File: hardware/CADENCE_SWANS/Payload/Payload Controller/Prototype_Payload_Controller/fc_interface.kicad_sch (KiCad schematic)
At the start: 9 parts

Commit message: clean up
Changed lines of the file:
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@@
 	(wire
 		(pts
-			(xy 44.45 82.55) (xy 52.07 82.55)
+			(xy 34.29 82.55) (xy 52.07 82.55)
 		)
 		(stroke
@@
 	(wire
 		(pts
-			(xy 44.45 69.85) (xy 53.34 69.85)
+			(xy 34.29 69.85) (xy 53.34 69.85)
 		)
 		(stroke
@@
 	(hierarchical_label "Payload_Rx"
 		(shape input)
-		(at 44.45 82.55 180)
+		(at 34.29 82.55 180)
 		(effects
 			(font
@@
 	(hierarchical_label "Payload_Tx"
 		(shape input)
-		(at 44.45 69.85 180)
+		(at 34.29 69.85 180)
 		(effects
 			(font

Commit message: minor updates
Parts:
- C2: value 10u -> 10uF
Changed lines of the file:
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@@
 			)
 		)
-		(property "Value" "10u"
+		(property "Value" "10uF"
 			(at 91.44 33.0262 0)
 			(effects

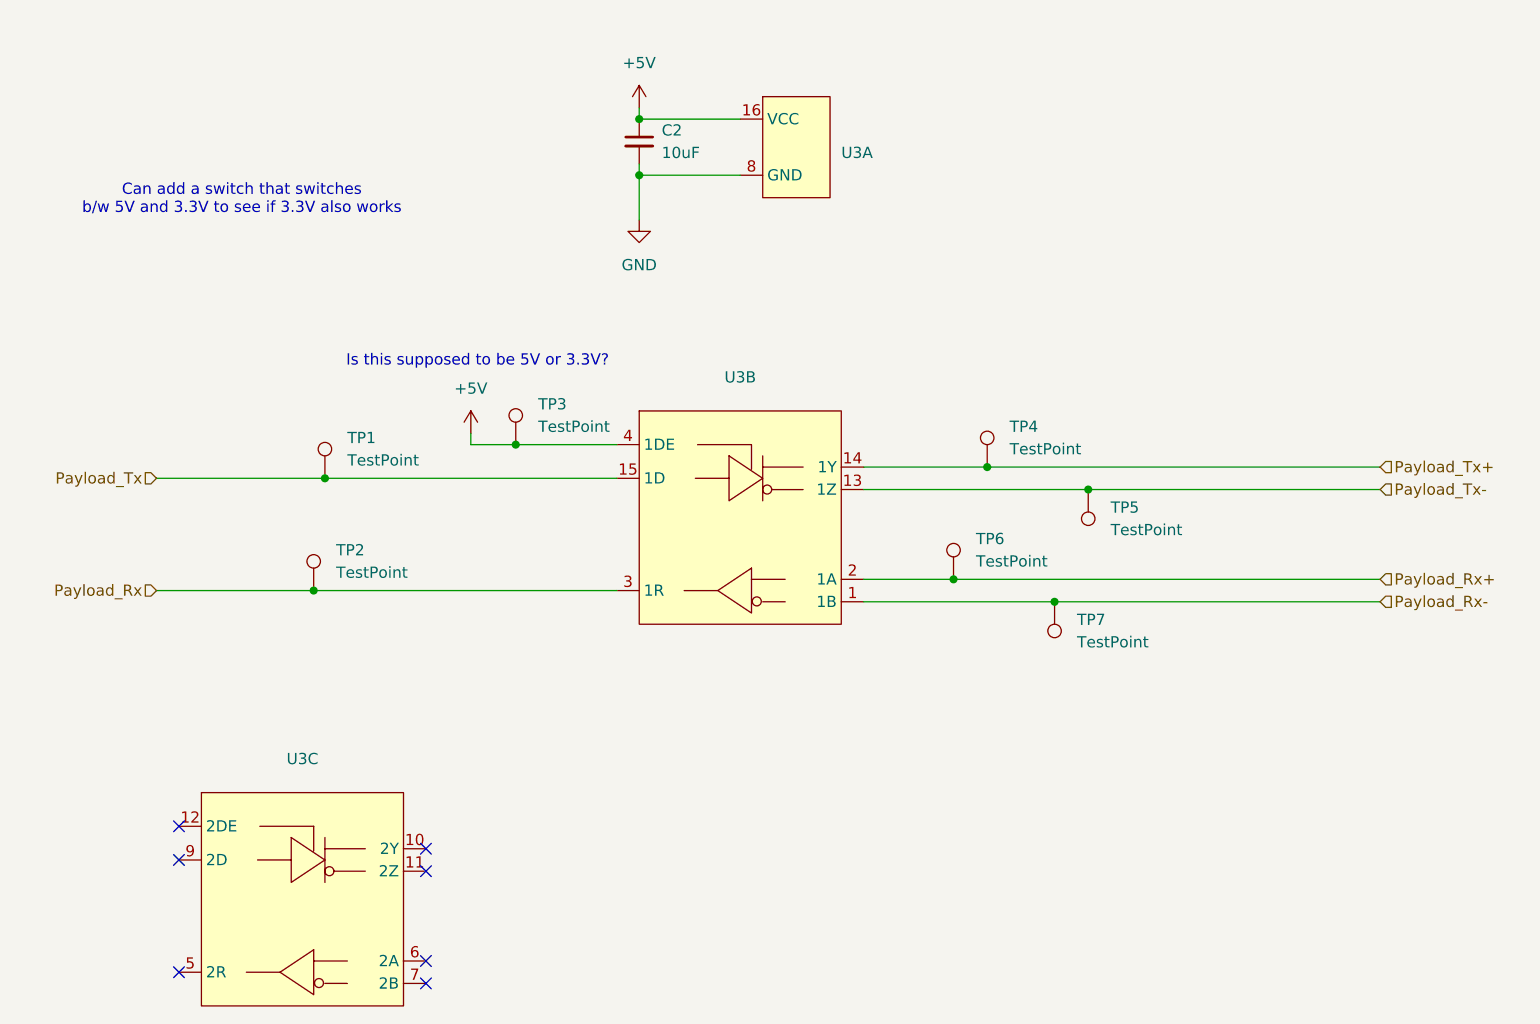
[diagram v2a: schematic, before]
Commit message: updated power regulators
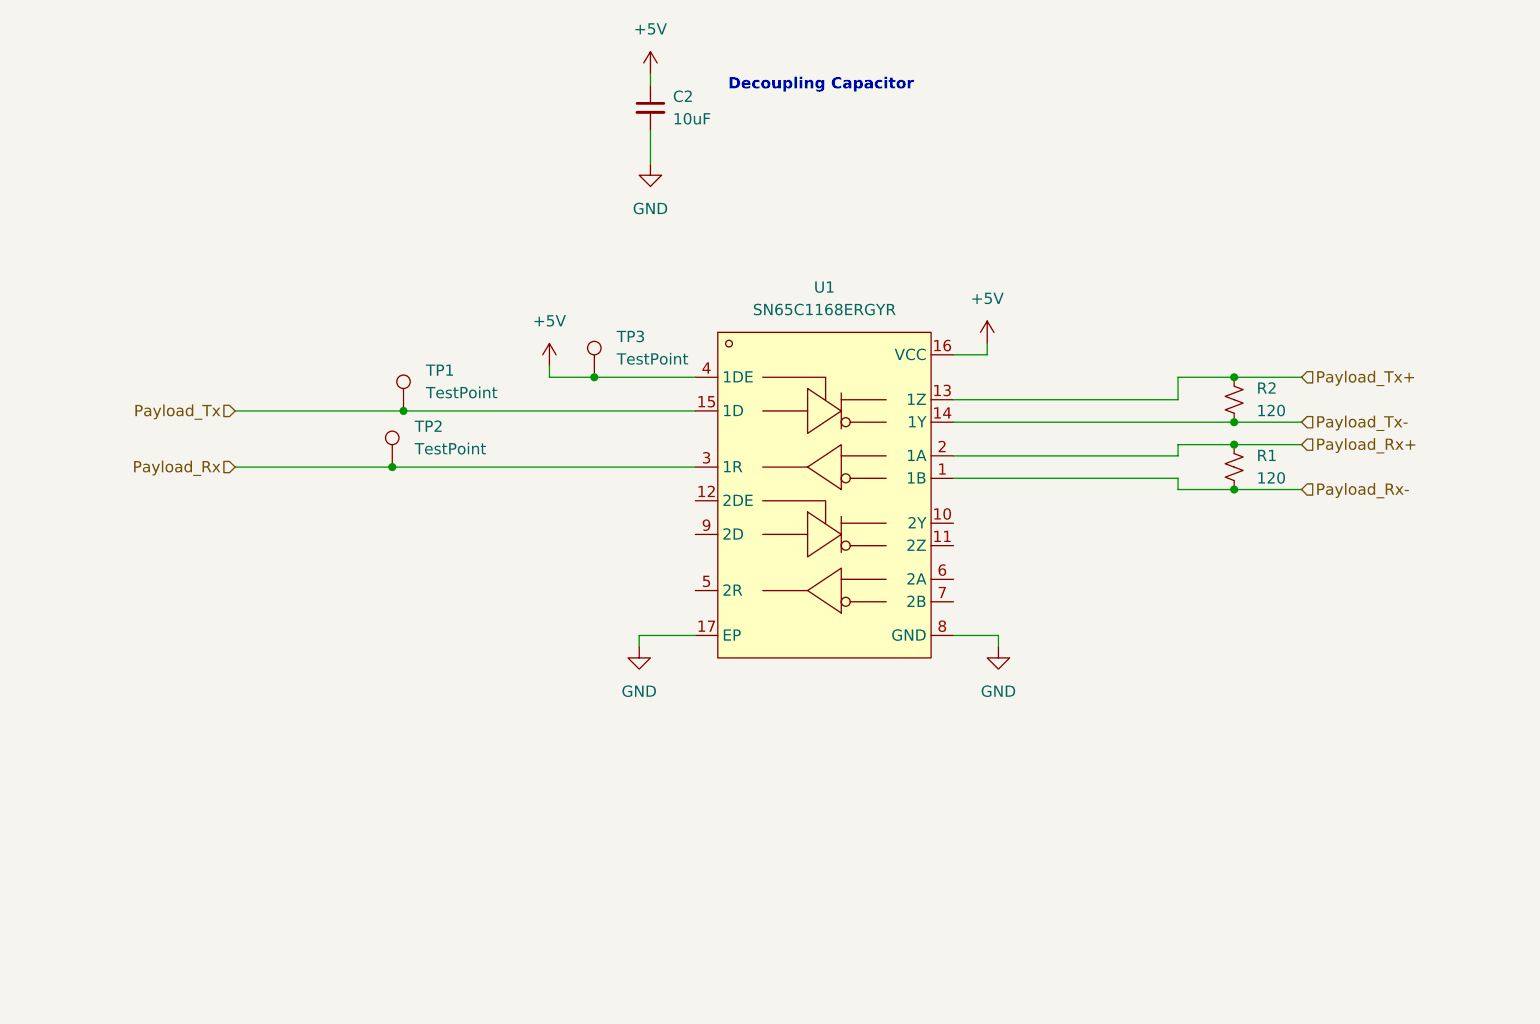
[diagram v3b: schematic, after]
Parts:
- removed TP4, TP5, TP6, TP7: TestPoint, symbol Connector:TestPoint
- removed U3: ~, symbol SN65C1168:SN65C1168
- added R1, R2: 120, symbol Device:R_Small_US
- added U1: SN65C1168ERGYR, easyeda2kicad:VQFN-16_L4.0-W3.5-P0.50-BL-EP, symbol CADENCE:SN65C1168ERGYR
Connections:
- net +5V: now also U1.16 (VCC), U1.4 (1DE)
- net GND: now also U1.17 (EP), U1.8 (GND)
- net Payload_Rx: now also U1.3 (1R)
- net Payload_Rx+: now also R1.1, U1.2 (1A)
- net Payload_Rx-: now also R1.2, U1.1 (1B)
- net Payload_Tx: now also U1.15 (1D)
- net Payload_Tx+: now also R2.1, U1.13 (1Z)
- net Payload_Tx-: now also R2.2, U1.14 (1Y)
- no-connect marks 7 -> 0
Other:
- note added: "Decoupling Capacitor"
- note removed: "Can add a switch that switches b/w 5V and 3.3V to see if 3.3V also works"
- note removed: "Is this supposed to be 5V or 3.3V?"
- moved on the sheet: C2, TP1, TP2, TP3

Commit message: cleaned up schematics and assigned footprints for resistors and capacitors
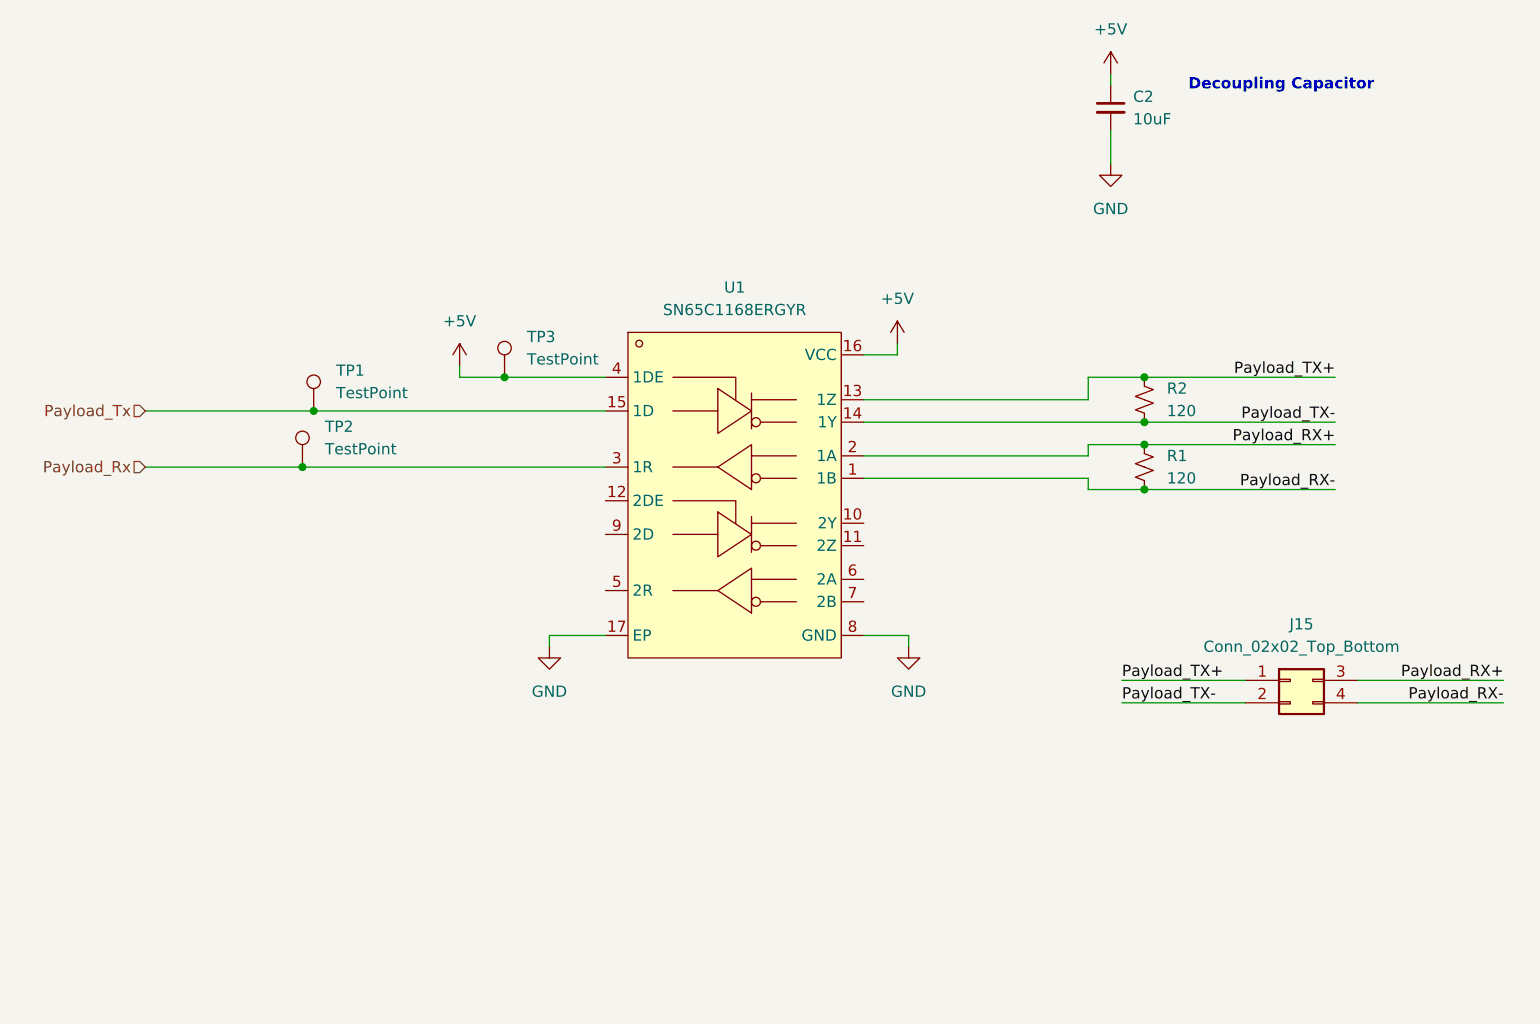
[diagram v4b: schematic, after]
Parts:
- added J15: Conn_02x02_Top_Bottom, symbol Connector_Generic:Conn_02x02_Top_Bottom
- C2: footprint (none) -> Capacitor_SMD:C_0603_1608Metric
- R1, R2: footprint (none) -> Resistor_SMD:R_0603_1608Metric
- TP1, TP2, TP3: footprint (none) -> TestPoint:TestPoint_Pad_1.0x1.0mm
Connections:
- net Payload_Rx+ renamed Payload_RX+
- net Payload_RX+: now also J15.3 (Pin_3)
- net Payload_Rx- renamed Payload_RX-
- net Payload_RX-: now also J15.4 (Pin_4)
- net Payload_Tx+ renamed Payload_TX+
- net Payload_TX+: now also J15.1 (Pin_1)
- net Payload_Tx- renamed Payload_TX-
- net Payload_TX-: now also J15.2 (Pin_2)
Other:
- moved on the sheet: C2, R1, R2, TP1, TP2, TP3, U1

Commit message: assigned more footprints
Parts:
- J15: footprint (none) -> Connector_Hirose:Hirose_DF11-4DP-2DSA_2x02_P2.00mm_Vertical
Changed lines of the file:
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@@
 			)
 		)
-		(property "Footprint" ""
+		(property "Footprint" "Connector_Hirose:Hirose_DF11-4DP-2DSA_2x02_P2.00mm_Vertical"
 			(at 162.56 92.71 0)
 			(effects

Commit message: removed termination resistor on transmitter end of RS422
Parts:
- removed R2: 120, Resistor_SMD:R_0603_1608Metric, symbol Device:R_Small_US
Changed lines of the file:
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@@
-	)
-	(junction
-		(at 146.05 58.42)
-		(diameter 0)
-		(color 0 0 0 0)
 	)
 	(junction
@@
 		(color 0 0 0 0)
 	)
-	(junction
-		(at 146.05 63.5)
-		(diameter 0)
-		(color 0 0 0 0)
-	)
 	(wire
 		(pts
@@
 	(wire
 		(pts
-			(xy 114.3 63.5) (xy 146.05 63.5)
+			(xy 114.3 63.5) (xy 167.64 63.5)
 		)
 		(stroke
@@
 	(wire
 		(pts
-			(xy 139.7 60.96) (xy 139.7 58.42)
-		)
-		(stroke
-			(width 0)
-			(type default)
-		)
-	)
-	(wire
-		(pts
 			(xy 118.11 55.88) (xy 118.11 54.61)
 		)
@@
 	(wire
 		(pts
-			(xy 139.7 58.42) (xy 146.05 58.42)
-		)
-		(stroke
-			(width 0)
-			(type default)
-		)
-	)
-	(wire
-		(pts
 			(xy 139.7 66.04) (xy 146.05 66.04)
 		)
@@
 	(wire
 		(pts
-			(xy 146.05 58.42) (xy 167.64 58.42)
-		)
-		(stroke
-			(width 0)
-			(type default)
-		)
-	)
-	(wire
-		(pts
-			(xy 146.05 63.5) (xy 167.64 63.5)
-		)
-		(stroke
-			(width 0)
-			(type default)
-		)
-	)
-	(wire
-		(pts
 			(xy 143.51 95.25) (xy 157.48 95.25)
 		)
@@
 	(wire
 		(pts
-			(xy 114.3 60.96) (xy 139.7 60.96)
+			(xy 114.3 60.96) (xy 167.64 60.96)
 		)
 		(stroke
@@
 	)
 	(label "Payload_TX+"
-		(at 167.64 58.42 180)
+		(at 167.64 60.96 180)
 		(effects
 			(font
@@
 					(unit 1)
 				)
-			)
-		)
-	)
-	(symbol
-		(lib_id "Device:R_Small_US")
-		(at 146.05 60.96 0)
-		(unit 1)
-		(exclude_from_sim no)
-		(in_bom yes)
-		(on_board yes)
-		(dnp no)
-		(fields_autoplaced yes)
-		(property "Reference" "R2"
-			(at 148.59 59.6899 0)
-			(effects
-				(font
-					(size 1.27 1.27)
-				)
-				(justify left)
-			)
-		)
-		(property "Value" "120"
-			(at 148.59 62.2299 0)
-			(effects
-				(font
-					(size 1.27 1.27)
-				)
-				(justify left)
-			)
-		)
-		(property "Footprint" "Resistor_SMD:R_0603_1608Metric"
-			(at 146.05 60.96 0)
-			(effects
-				(font
-					(size 1.27 1.27)
-				)
-				(hide yes)
-			)
-		)
-		(property "Datasheet" "~"
-			(at 146.05 60.96 0)
-			(effects
-				(font
-					(size 1.27 1.27)
-				)
-				(hide yes)
-			)
-		)
-		(property "Description" "Resistor, small US symbol"
-			(at 146.05 60.96 0)
-			(effects
-				(font
-					(size 1.27 1.27)
-				)
-				(hide yes)
-			)
-		)
-		(pin "1"
-		)
-		(pin "2"
-		)
-		(instances
-			(project "Payload_Controller_EM"
-				(path "/866a965d-c307-40b7-9977-69e77fc0dc82/7acf6d3b-d272-4af5-ad05-5ed10a438eac"
-					(reference "R2")
-					(unit 1)
-				)

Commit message: linked more footprints
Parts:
- U1: footprint easyeda2kicad:VQFN-16_L4.0-W3.5-P0.50-BL-EP -> Package_SO:SOP-16_4.55x10.3mm_P1.27mm
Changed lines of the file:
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@@
 			)
 		)
-		(property "Footprint" "easyeda2kicad:VQFN-16_L4.0-W3.5-P0.50-BL-EP"
+		(property "Footprint" "Package_SO:SOP-16_4.55x10.3mm_P1.27mm"
 			(at 94.234 94.742 0)
 			(effects

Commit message: resolved ERC errors
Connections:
- no-connect marks 0 -> 7
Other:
- moved on the sheet: C2
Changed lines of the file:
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@@
 	(text "Decoupling Capacitor"
 		(exclude_from_sim no)
-		(at 161.544 25.4 0)
+		(at 151.384 33.02 0)
 		(effects
 			(font
@@
 		(color 0 0 0 0)
 	)
+	(no_connect
+		(at 85.09 82.55)
+	)
+	(no_connect
+		(at 85.09 76.2)
+	)
+	(no_connect
+		(at 114.3 77.47)
+	)
+	(no_connect
+		(at 114.3 74.93)
+	)
+	(no_connect
+		(at 85.09 72.39)
+	)
+	(no_connect
+		(at 114.3 81.28)
+	)
+	(no_connect
+		(at 114.3 83.82)
+	)
 	(wire
 		(pts
@@
 	(wire
 		(pts
-			(xy 142.24 24.13) (xy 142.24 25.4)
+			(xy 132.08 31.75) (xy 132.08 33.02)
 		)
 		(stroke
@@
 	(wire
 		(pts
-			(xy 142.24 30.48) (xy 142.24 34.29)
+			(xy 132.08 38.1) (xy 132.08 41.91)
 		)
 		(stroke
@@
 	(symbol
 		(lib_id "Device:C_Small")
-		(at 142.24 27.94 0)
+		(at 132.08 35.56 0)
 		(unit 1)
 		(exclude_from_sim no)
@@
 		(dnp no)
 		(property "Reference" "C2"
-			(at 144.78 26.6762 0)
+			(at 134.62 34.2962 0)
 			(effects
 				(font
@@
 		)
 		(property "Value" "10uF"
-			(at 144.78 29.2162 0)
+			(at 134.62 36.8362 0)
 			(effects
 				(font
@@
 		)
 		(property "Footprint" "Capacitor_SMD:C_0603_1608Metric"
-			(at 142.24 27.94 0)
+			(at 132.08 35.56 0)
 			(effects
 				(font
@@
 		)
 		(property "Datasheet" "~"
-			(at 142.24 27.94 0)
+			(at 132.08 35.56 0)
 			(effects
 				(font
@@
 		)
 		(property "Description" "Unpolarized capacitor, small symbol"
-			(at 142.24 27.94 0)
+			(at 132.08 35.56 0)
 			(effects
 				(font
@@
 	(symbol
 		(lib_id "power:GND")
-		(at 142.24 34.29 0)
+		(at 132.08 41.91 0)
 		(unit 1)
 		(exclude_from_sim no)
@@
 		(fields_autoplaced yes)
 		(property "Reference" "#PWR015"
-			(at 142.24 40.64 0)
+			(at 132.08 48.26 0)
 			(effects
 				(font
@@
 		)
 		(property "Value" "GND"
-			(at 142.24 39.37 0)
+			(at 132.08 46.99 0)
 			(effects
 				(font
@@
 		)
 		(property "Footprint" ""
-			(at 142.24 34.29 0)
+			(at 132.08 41.91 0)
 			(effects
 				(font
@@
 		)
 		(property "Datasheet" ""
-			(at 142.24 34.29 0)
+			(at 132.08 41.91 0)
 			(effects
 				(font
@@
 		)
 		(property "Description" "Power symbol creates a global label with name \"GND\" , ground"
-			(at 142.24 34.29 0)
+			(at 132.08 41.91 0)
 			(effects
 				(font
@@
 	(symbol
 		(lib_id "power:+5V")
-		(at 142.24 24.13 0)
+		(at 132.08 31.75 0)
 		(unit 1)
 		(exclude_from_sim no)
@@
 		(fields_autoplaced yes)
 		(property "Reference" "#PWR016"
-			(at 142.24 27.94 0)
+			(at 132.08 35.56 0)
 			(effects
 				(font
@@
 		)
 		(property "Value" "+5V"
-			(at 142.24 19.05 0)
+			(at 132.08 26.67 0)
 			(effects
 				(font
@@
 		)
 		(property "Footprint" ""
-			(at 142.24 24.13 0)
+			(at 132.08 31.75 0)
 			(effects
 				(font
@@
 		)
 		(property "Datasheet" ""
-			(at 142.24 24.13 0)
+			(at 132.08 31.75 0)
 			(effects
 				(font
@@
 		)
 		(property "Description" "Power symbol creates a global label with name \"+5V\""
-			(at 142.24 24.13 0)
-			(effects
-				(font
+			(at 132.08 31.75 0)
+			(effects
+				(font
